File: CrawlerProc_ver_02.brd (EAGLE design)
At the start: 57 parts, among them U1 MIC5335-SPYMT, U10 ECS-160-8, U11 ANTENNA, U12 ANTENNA-CHIP, U2 MIC5320-JGYML, U3 ITG-3200, U4 AT86RF231-ZU, U5 AT45DB321D, U6 ECS-2033, U8 ADXL345-LGA12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

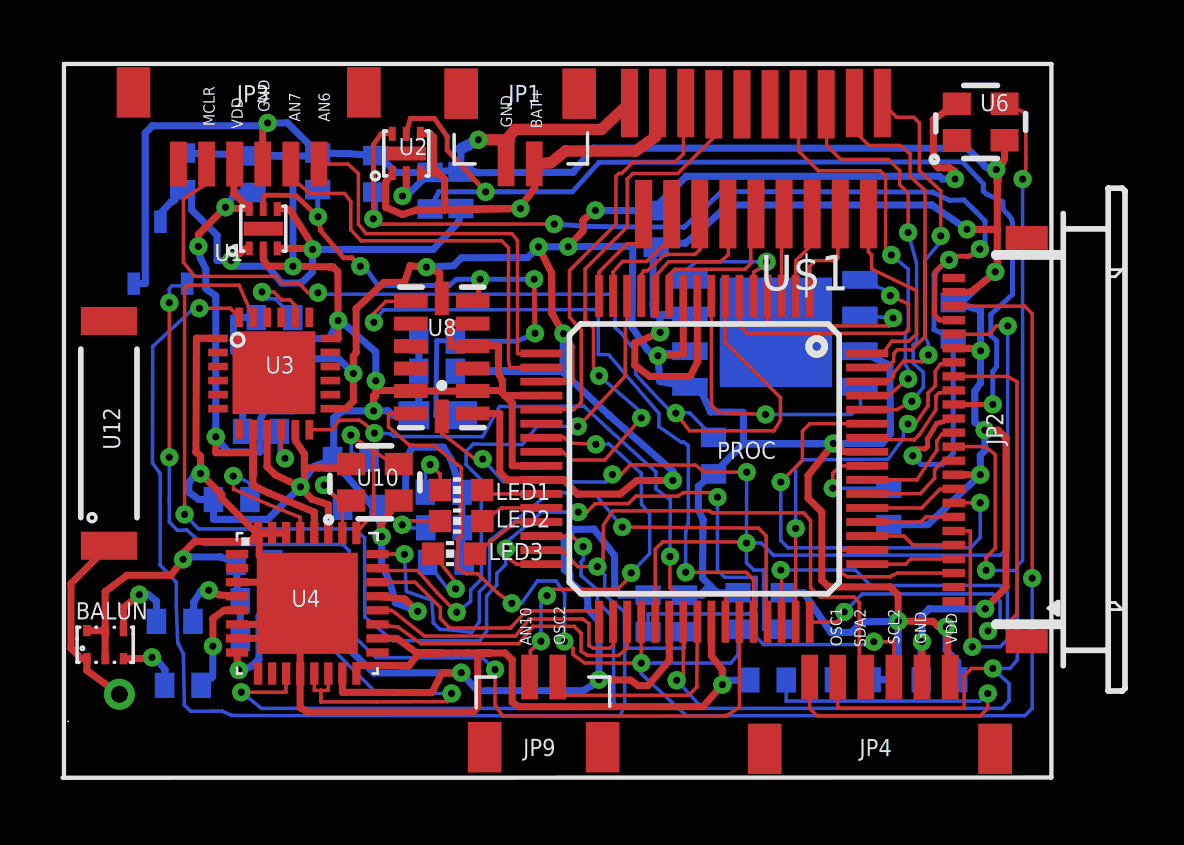
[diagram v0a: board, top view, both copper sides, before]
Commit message: Added dimensions
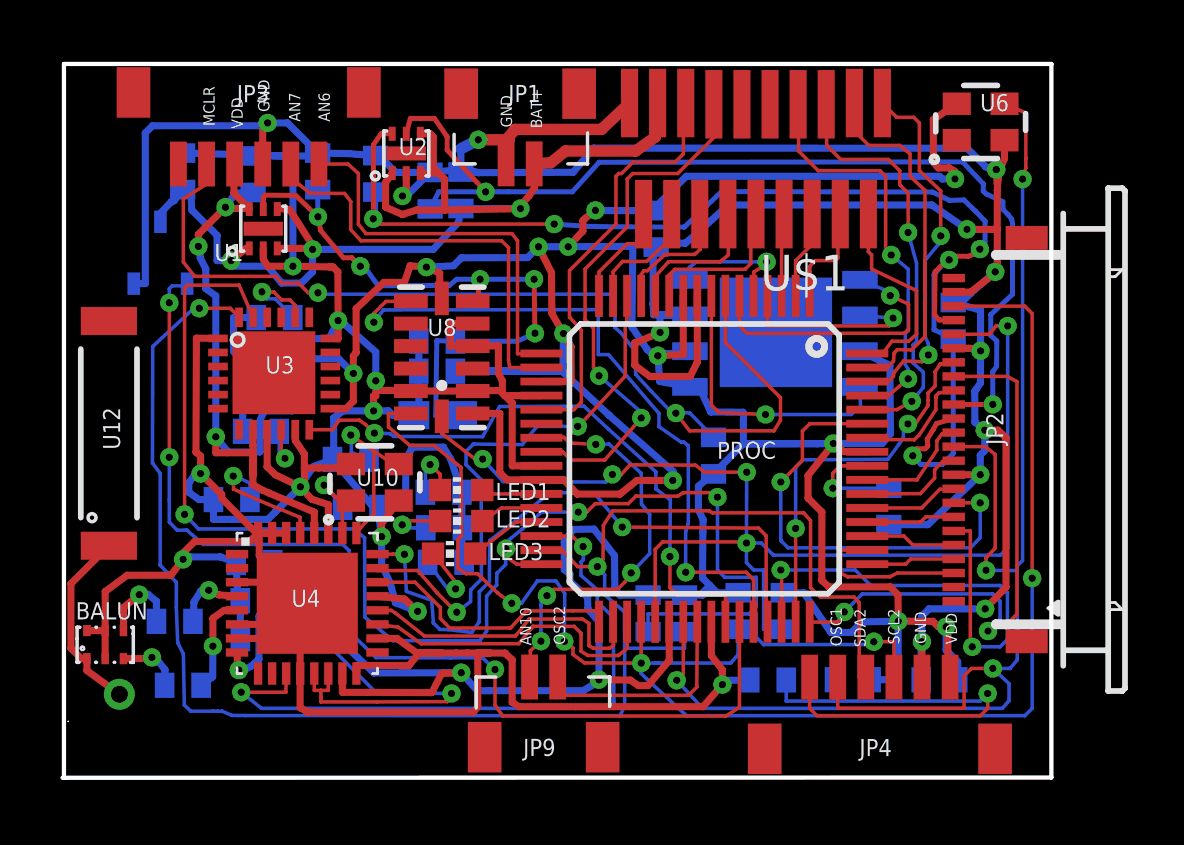
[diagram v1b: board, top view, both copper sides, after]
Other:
- board outline added: 35.2 x 25.4 mm
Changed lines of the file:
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@@
 <board>
 <plain>
-<wire x1="-0.2" y1="-2.01" x2="35" y2="-2" width="0.1524" layer="21"/>
-<wire x1="35" y1="-2" x2="35" y2="23.4" width="0.1524" layer="21"/>
-<wire x1="35" y1="23.4" x2="-0.15" y2="23.4" width="0.1524" layer="21"/>
-<wire x1="-0.15" y1="23.4" x2="-0.15" y2="-2" width="0.1524" layer="21"/>
+<wire x1="-0.2" y1="-2.01" x2="35" y2="-2" width="0.1524" layer="20"/>
+<wire x1="35" y1="-2" x2="35" y2="23.4" width="0.1524" layer="20"/>
+<wire x1="35" y1="23.4" x2="-0.15" y2="23.4" width="0.1524" layer="20"/>
+<wire x1="-0.15" y1="23.4" x2="-0.15" y2="-2" width="0.1524" layer="20"/>
 <wire x1="0.01" y1="0" x2="0" y2="0" width="0" layer="20"/>
 <wire x1="0" y1="0" x2="0" y2="-0.01" width="0" layer="20"/>

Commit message: Updated with routing for SPI breakout
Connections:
- removed net N$2: PROC.6, U5.1
- removed net N$42: PROC.4, U5.2
- removed net N$45: PROC.5, U5.8
- removed net PWM2L: PROC.62, U$1.1
- new net SCK2: PROC.4, PROC.62, U$1.1, U5.2
- new net SDI2: PROC.5, U$1.9, U5.8
- new net SDO2: PROC.6, U$1.11, U5.1
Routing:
- net SCK2: track 0.00 -> 20.2 mm, vias 0 -> 3
- net PWM2L: track 13.1 -> 0.00 mm, vias 2 -> 0
- net SDO2: track 0.00 -> 10.5 mm, vias 0 -> 1
- net N$2: track 10.5 -> 0.00 mm, vias 1 -> 0
- net N$42: track 7.17 -> 0.00 mm, vias 1 -> 0
- net SDI2: track 0.00 -> 4.93 mm, vias 0 -> 1
- net N$45: track 4.93 -> 0.00 mm, vias 1 -> 0
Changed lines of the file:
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@@
 <layer number="17" name="Pads" color="2" fill="1" visible="yes" active="yes"/>
 <layer number="18" name="Vias" color="2" fill="1" visible="yes" active="yes"/>
-<layer number="19" name="Unrouted" color="6" fill="1" visible="no" active="yes"/>
+<layer number="19" name="Unrouted" color="6" fill="1" visible="yes" active="yes"/>
 <layer number="20" name="Dimension" color="15" fill="1" visible="yes" active="yes"/>
 <layer number="21" name="tPlace" color="16" fill="1" visible="yes" active="yes"/>
@@
 <via x="7.7176" y="9.3593" extent="1-16" drill="0.254" diameter="0.6604"/>
 </signal>
-<signal name="N$45">
-<contactref element="U5" pad="8"/>
-<contactref element="PROC" pad="5"/>
-<wire x1="24.7135" y1="16.1726" x2="24.8633" y2="16.3563" width="0.127" layer="1"/>
-<wire x1="24.4056" y1="15.9956" x2="24.7482" y2="16.1999" width="0.127" layer="1"/>
-<wire x1="24.7482" y1="16.1999" x2="24.6595" y2="16.1438" width="0.127" layer="1"/>
-<wire x1="24.6595" y1="16.1438" x2="24.7135" y2="16.1726" width="0.127" layer="1"/>
-<wire x1="24.3956" y1="15.1444" x2="24.4056" y2="15.9956" width="0.127" layer="1"/>
-<wire x1="22.3516" y1="16.3563" x2="24.8633" y2="16.3563" width="0.127" layer="16"/>
-<wire x1="22.1314" y1="16.1661" x2="22.3516" y2="16.3563" width="0.127" layer="16"/>
-<wire x1="22.1113" y1="16.1461" x2="22.1314" y2="16.1661" width="0.127" layer="16"/>
-<wire x1="22.1113" y1="16.1556" x2="22.1113" y2="16.1461" width="0.127" layer="16"/>
-<wire x1="22.134" y1="15.7156" x2="22.1113" y2="16.1556" width="0.127" layer="16"/>
-<via x="24.8633" y="16.3563" extent="1-16" drill="0.254" diameter="0.6604"/>
-</signal>
 <signal name="RF1">
 <contactref element="PROC" pad="59"/>
@@
 <wire x1="30.8902" y1="11.5862" x2="30.988" y2="11.684" width="0.127" layer="1"/>
 <wire x1="30.988" y1="11.684" x2="31.5206" y2="11.778" width="0.127" layer="1"/>
-</signal>
-<signal name="N$42">
-<contactref element="U5" pad="2"/>
-<contactref element="PROC" pad="4"/>
-<wire x1="29.2293" y1="14.0741" x2="29.3625" y2="14.3543" width="0.127" layer="1"/>
-<wire x1="24.8956" y1="14.0741" x2="29.2293" y2="14.0741" width="0.127" layer="1"/>
-<wire x1="24.8956" y1="15.1444" x2="24.8956" y2="14.0741" width="0.127" layer="1"/>
-<wire x1="29.3625" y1="14.3543" x2="29.4982" y2="14.3456" width="0.127" layer="16"/>
-<wire x1="29.4982" y1="14.3456" x2="28.184" y2="14.4456" width="0.127" layer="16"/>
-<via x="29.3625" y="14.3543" extent="1-16" drill="0.254" diameter="0.6604"/>
 </signal>
 <signal name="N$48">
@@
 <via x="21.6316" y="10.971" extent="1-16" drill="0.254" diameter="0.6604"/>
 <via x="8.8899" y="15.2557" extent="1-16" drill="0.254" diameter="0.6604"/>
-</signal>
-<signal name="N$2">
-<contactref element="U5" pad="1"/>
-<contactref element="PROC" pad="6"/>
-<wire x1="29.9156" y1="14.849" x2="29.2625" y2="15.1553" width="0.127" layer="1"/>
-<wire x1="29.9157" y1="13.9552" x2="29.9156" y2="14.849" width="0.127" layer="1"/>
-<wire x1="29.7697" y1="13.8138" x2="29.9157" y2="13.9552" width="0.127" layer="1"/>
-<wire x1="24.1641" y1="13.8138" x2="29.7697" y2="13.8138" width="0.127" layer="1"/>
-<wire x1="23.8956" y1="14.0823" x2="24.1641" y2="13.8138" width="0.127" layer="1"/>
-<wire x1="23.8956" y1="15.1444" x2="23.8956" y2="14.0823" width="0.127" layer="1"/>
-<wire x1="29.2625" y1="15.1553" x2="29.4992" y2="15.1856" width="0.127" layer="16"/>
-<wire x1="29.4992" y1="15.1856" x2="28.184" y2="15.7156" width="0.127" layer="16"/>
-<via x="29.2625" y="15.1553" extent="1-16" drill="0.254" diameter="0.6604"/>
 </signal>
 <signal name="BAT+" class="1">
@@
 <via x="29.9" y="17.4" extent="1-16" drill="0.254"/>
 </signal>
-<signal name="PWM2L">
+<signal name="SCK2">
 <contactref element="PROC" pad="62"/>
 <contactref element="U$1" pad="1"/>
@@
 <via x="30.62" y="13.04" extent="1-16" drill="0.254"/>
 <via x="31.06" y="17.28" extent="1-16" drill="0.254"/>
+<contactref element="U5" pad="2"/>
+<contactref element="PROC" pad="4"/>
+<wire x1="29.2293" y1="14.0741" x2="29.3625" y2="14.3543" width="0.127" layer="1"/>
+<wire x1="24.8956" y1="14.0741" x2="29.2293" y2="14.0741" width="0.127" layer="1"/>
+<wire x1="24.8956" y1="15.1444" x2="24.8956" y2="14.0741" width="0.127" layer="1"/>
+<wire x1="29.3625" y1="14.3543" x2="29.4982" y2="14.3456" width="0.127" layer="16"/>
+<wire x1="29.4982" y1="14.3456" x2="28.184" y2="14.4456" width="0.127" layer="16"/>
+<via x="29.3625" y="14.3543" extent="1-16" drill="0.254" diameter="0.6604"/>
+<wire x1="29.4982" y1="14.3456" x2="30.5" y2="13.7" width="0" layer="19" extent="16-16"/>
 </signal>
 <signal name="PWM4L">
@@
 <contactref element="PROC" pad="22"/>
 </signal>
+<signal name="SDI2">
+<contactref element="U$1" pad="9"/>
+<contactref element="U5" pad="8"/>
+<contactref element="PROC" pad="5"/>
+<wire x1="24.7135" y1="16.1726" x2="24.8633" y2="16.3563" width="0.127" layer="1"/>
+<wire x1="24.4056" y1="15.9956" x2="24.7482" y2="16.1999" width="0.127" layer="1"/>
+<wire x1="24.7482" y1="16.1999" x2="24.6595" y2="16.1438" width="0.127" layer="1"/>
+<wire x1="24.6595" y1="16.1438" x2="24.7135" y2="16.1726" width="0.127" layer="1"/>
+<wire x1="24.3956" y1="15.1444" x2="24.4056" y2="15.9956" width="0.127" layer="1"/>
+<wire x1="22.3516" y1="16.3563" x2="24.8633" y2="16.3563" width="0.127" layer="16"/>
+<wire x1="22.1314" y1="16.1661" x2="22.3516" y2="16.3563" width="0.127" layer="16"/>
+<wire x1="22.1113" y1="16.1461" x2="22.1314" y2="16.1661" width="0.127" layer="16"/>
+<wire x1="22.1113" y1="16.1556" x2="22.1113" y2="16.1461" width="0.127" layer="16"/>
+<wire x1="22.134" y1="15.7156" x2="22.1113" y2="16.1556" width="0.127" layer="16"/>
+<via x="24.8633" y="16.3563" extent="1-16" drill="0.254" diameter="0.6604"/>
+<wire x1="24.8633" y1="16.3563" x2="24.984" y2="21.964" width="0" layer="19" extent="1-1"/>
+</signal>
+<signal name="SDO2">
+<contactref element="U$1" pad="11"/>
+<contactref element="U5" pad="1"/>
+<contactref element="PROC" pad="6"/>
+<wire x1="29.9156" y1="14.849" x2="29.2625" y2="15.1553" width="0.127" layer="1"/>
+<wire x1="29.9157" y1="13.9552" x2="29.9156" y2="14.849" width="0.127" layer="1"/>
+<wire x1="29.7697" y1="13.8138" x2="29.9157" y2="13.9552" width="0.127" layer="1"/>
+<wire x1="24.1641" y1="13.8138" x2="29.7697" y2="13.8138" width="0.127" layer="1"/>
+<wire x1="23.8956" y1="14.0823" x2="24.1641" y2="13.8138" width="0.127" layer="1"/>
+<wire x1="23.8956" y1="15.1444" x2="23.8956" y2="14.0823" width="0.127" layer="1"/>
+<wire x1="29.2625" y1="15.1553" x2="29.4992" y2="15.1856" width="0.127" layer="16"/>
+<wire x1="29.4992" y1="15.1856" x2="28.184" y2="15.7156" width="0.127" layer="16"/>
+<via x="29.2625" y="15.1553" extent="1-16" drill="0.254" diameter="0.6604"/>
+<wire x1="23.8956" y1="15.1444" x2="23.984" y2="21.964" width="0" layer="19" extent="1-1"/>
+</signal>
 </signals>

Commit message: SPI breakout routing changes and Freerouter script
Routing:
- net GND: track 269.6 -> 238.2 mm, vias 22 -> 17
- net SCL2: track 56.1 -> 82.4 mm, vias 5 -> 6
- net VDD: track 198.8 -> 176.5 mm, vias 18 -> 15
- net INT3: track 25.0 -> 44.6 mm
- net AN5: track 5.65 -> 23.2 mm, vias 0 -> 4
- net SDO2: track 10.5 -> 24.2 mm
- net VEE: track 35.8 -> 48.3 mm
- net N$57: track 17.0 -> 5.34 mm
- net N$28: track 14.0 -> 4.49 mm
- net RD0: track 18.0 -> 8.67 mm
- net SCL1: track 44.7 -> 37.5 mm, vias 5 -> 4
- net SDA1: track 55.9 -> 48.7 mm, vias 4 -> 2
- net RF1: track 16.2 -> 9.02 mm
- net VCC: track 44.1 -> 37.3 mm, vias 5 -> 4
- net OSC1: track 52.2 -> 58.6 mm, vias 4 -> 5
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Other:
- board size 35.2 x 25.4 mm -> 35.6 x 25.9 mm

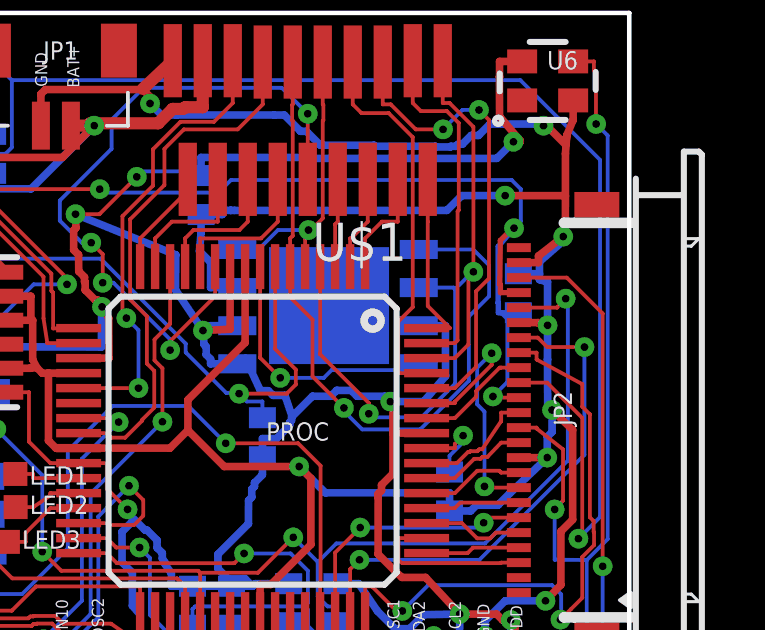
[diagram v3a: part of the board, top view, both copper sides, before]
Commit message: Fixed error that connected PWM2L to the SCK2 line
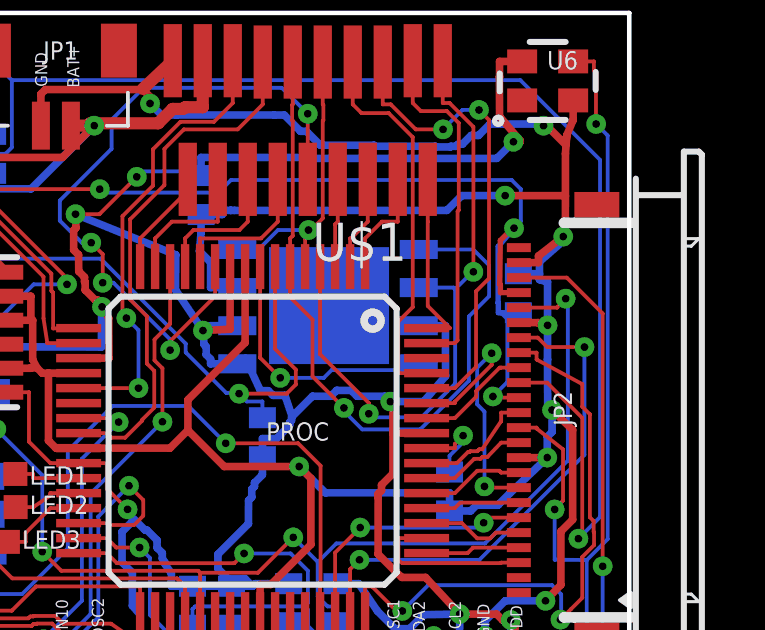
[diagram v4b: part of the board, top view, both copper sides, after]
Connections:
- new net PWM2L: PROC.62
- net SCK2: no longer PROC.62
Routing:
- net SCK2: track 25.9 -> 21.8 mm
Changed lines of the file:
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@@
 </signal>
 <signal name="SCK2">
-<contactref element="PROC" pad="62"/>
 <contactref element="U$1" pad="1"/>
 <contactref element="U5" pad="2"/>
@@
 <wire x1="28.27601875" y1="10.12261875" x2="26.63566875" y2="10.12261875" width="0.127" layer="16"/>
 <wire x1="26.63566875" y1="10.12261875" x2="26.51868125" y2="10.239609375" width="0.127" layer="16"/>
-<wire x1="29.386109375" y1="12.0944" x2="29.83943125" y2="12.54771875" width="0.127" layer="1"/>
-<wire x1="29.83943125" y1="12.54771875" x2="29.83943125" y2="14.804309375" width="0.127" layer="1"/>
-<wire x1="29.83943125" y1="14.804309375" x2="30.00483125" y2="14.969709375" width="0.127" layer="1"/>
 <wire x1="28.184" y1="14.4456" x2="29.34815" y2="14.4456" width="0.127" layer="16"/>
 <wire x1="29.34815" y1="14.4456" x2="29.398340625" y2="14.395409375" width="0.127" layer="16"/>
@@
 <via x="30.00483125" y="14.969709375" extent="1-16" drill="0.254" diameter="0.6604"/>
 <wire x1="28.984" y1="22.009" x2="28.984" y2="20.598490625" width="0.127" layer="1"/>
-<wire x1="28.4456" y1="12.0944" x2="29.386109375" y2="12.0944" width="0.127" layer="1"/>
 </signal>
 <signal name="PWM4L">
@@
 <wire x1="23.8956" y1="15.1444" x2="23.8956" y2="16.084909375" width="0.127" layer="1"/>
 </signal>
+<signal name="PWM2L">
+<contactref element="PROC" pad="62"/>
+</signal>
 </signals>
